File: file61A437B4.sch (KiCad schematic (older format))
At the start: 2 parts, among them J1 DB37_Male

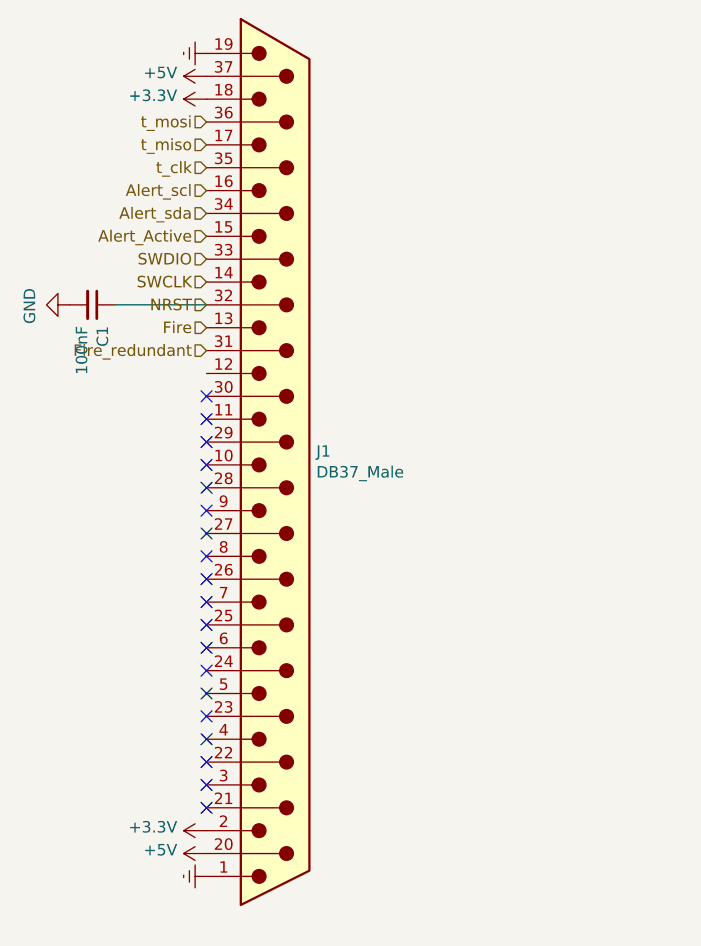
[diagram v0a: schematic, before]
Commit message: Updated PCB
Finalized most of the charges board and PCB
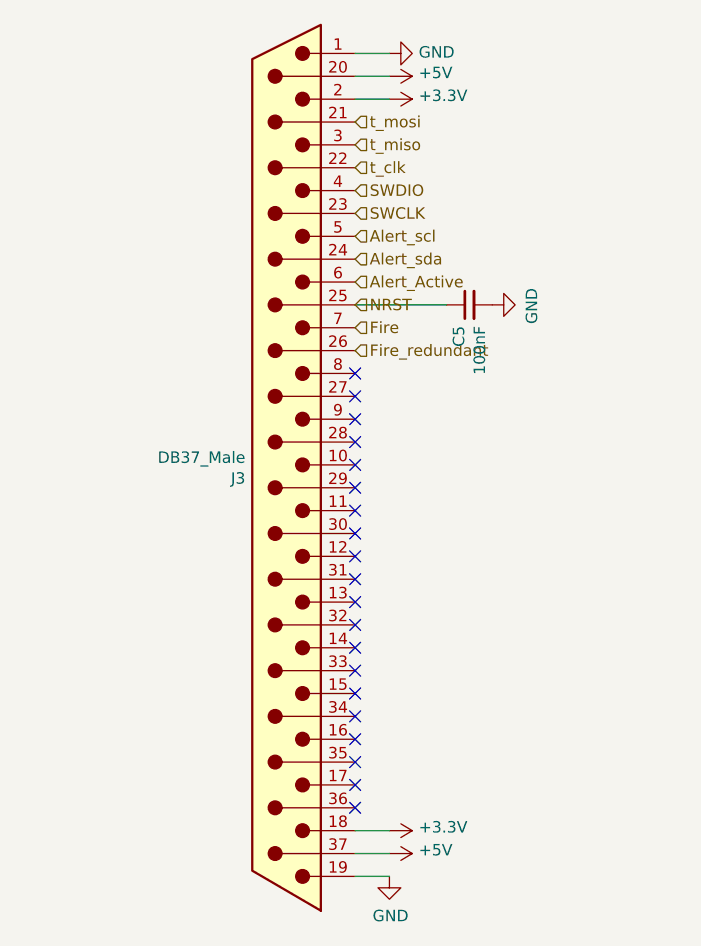
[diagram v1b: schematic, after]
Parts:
- C5: renamed from C1; footprint (none) -> Capacitor_SMD:C_0603_1608Metric
- J3: renamed from J1; footprint (none) -> Connector_Dsub:DSUB-37_Male_Horizontal_P2.77x2.54mm_EdgePinOffset9.40mm
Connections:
- net Earth is gone; now on net GND: J3.1, J3.19
- net Alert_Active: now also J3.6; no longer J3.15
- net Alert_scl: now also J3.5; no longer J3.16
- net Alert_sda: now also J3.24; no longer J3.34
- net Fire: now also J3.7; no longer J3.13
- net Fire_redundant: now also J3.26; no longer J3.31
- net NRST: now also J3.25; no longer J3.32
- net SWCLK: now also J3.23; no longer J3.14
- net SWDIO: now also J3.4; no longer J3.33
- net t_clk: now also J3.22; no longer J3.35
- net t_miso: now also J3.3; no longer J3.17
- net t_mosi: now also J3.21; no longer J3.36
- no-connect marks 19 -> 20
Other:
- moved on the sheet: C5, J3
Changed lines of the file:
@@
 $Descr A4 11693 8268
 encoding utf-8
-Sheet 4 4
+Sheet 2 4
 Title ""
 Date ""
@@
 $EndDescr
 $Comp
-L Connector:DB37_Male J1
+L Connector:DB37_Male J3
 U 1 1 61A44CBA
-P 5550 3300
-F 0 "J1" H 5730 3359 50  0000 L CNN
-F 1 "DB37_Male" H 5730 3268 50  0000 L CNN
-F 2 "" H 5550 3300 50  0001 C CNN
-F 3 " ~" H 5550 3300 50  0001 C CNN
-	1    5550 3300
-	1    0    0    -1
+P 5600 3300
+F 0 "J3" H 5780 3359 50  0000 L CNN
+F 1 "DB37_Male" H 5780 3268 50  0000 L CNN
+F 2 "Connector_Dsub:DSUB-37_Male_Horizontal_P2.77x2.54mm_EdgePinOffset9.40mm" H 5600 3300 50  0001 C CNN
+F 3 " ~" H 5600 3300 50  0001 C CNN
+	1    5600 3300
+	-1   0    0    1
 $EndComp
-$Comp
-L power:Earth #PWR0104
-U 1 1 61A472F3
-P 5250 1500
-F 0 "#PWR0104" H 5250 1250 50  0001 C CNN
-F 1 "Earth" H 5250 1350 50  0001 C CNN
-F 2 "" H 5250 1500 50  0001 C CNN
-F 3 "~" H 5250 1500 50  0001 C CNN
-	1    5250 1500
-	0    1    1    0
-$EndComp
-$Comp
-L power:Earth #PWR0105
-U 1 1 61A486AF
-P 5250 5100
-F 0 "#PWR0105" H 5250 4850 50  0001 C CNN
-F 1 "Earth" H 5250 4950 50  0001 C CNN
-F 2 "" H 5250 5100 50  0001 C CNN
-F 3 "~" H 5250 5100 50  0001 C CNN
-	1    5250 5100
-	0    1    1    0
-$EndComp
-$Comp
-L power:+5V #PWR0137
-U 1 1 61A491E6
-P 5250 1600
-F 0 "#PWR0137" H 5250 1450 50  0001 C CNN
-F 1 "+5V" V 5265 1728 50  0000 L CNN
-F 2 "" H 5250 1600 50  0001 C CNN
-F 3 "" H 5250 1600 50  0001 C CNN
-	1    5250 1600
-	0    -1   -1   0
-$EndComp
-$Comp
-L power:+5V #PWR0138
-U 1 1 61A49AB4
-P 5250 5000
-F 0 "#PWR0138" H 5250 4850 50  0001 C CNN
-F 1 "+5V" V 5265 5128 50  0000 L CNN
-F 2 "" H 5250 5000 50  0001 C CNN
-F 3 "" H 5250 5000 50  0001 C CNN
-	1    5250 5000
-	0    -1   -1   0
-$EndComp
-$Comp
-L power:+3.3V #PWR0139
-U 1 1 61A4A3FB
-P 5250 1700
-F 0 "#PWR0139" H 5250 1550 50  0001 C CNN
-F 1 "+3.3V" V 5265 1828 50  0000 L CNN
-F 2 "" H 5250 1700 50  0001 C CNN
-F 3 "" H 5250 1700 50  0001 C CNN
-	1    5250 1700
-	0    -1   -1   0
-$EndComp
-$Comp
-L power:+3.3V #PWR0140
-U 1 1 61A4AB5D
-P 5250 4900
-F 0 "#PWR0140" H 5250 4750 50  0001 C CNN
-F 1 "+3.3V" V 5265 5028 50  0000 L CNN
-F 2 "" H 5250 4900 50  0001 C CNN
-F 3 "" H 5250 4900 50  0001 C CNN
-	1    5250 4900
-	0    -1   -1   0
-$EndComp
-Text HLabel 5250 1800 0    50   Input ~ 0
+Text HLabel 5900 1800 2    50   Input ~ 0
 t_mosi
-Text HLabel 5250 1900 0    50   Input ~ 0
+Text HLabel 5900 1900 2    50   Input ~ 0
 t_miso
-Text HLabel 5250 2000 0    50   Input ~ 0
+Text HLabel 5900 2000 2    50   Input ~ 0
 t_clk
-Text HLabel 5250 2100 0    50   Input ~ 0
+Text HLabel 5900 2300 2    50   Input ~ 0
 Alert_scl
-Text HLabel 5250 2200 0    50   Input ~ 0
+Text HLabel 5900 2400 2    50   Input ~ 0
 Alert_sda
-Text HLabel 5250 2300 0    50   Input ~ 0
+Text HLabel 5900 2500 2    50   Input ~ 0
 Alert_Active
-Text HLabel 5250 2400 0    50   Input ~ 0
+Text HLabel 5900 2100 2    50   Input ~ 0
 SWDIO
-Text HLabel 5250 2500 0    50   Input ~ 0
+Text HLabel 5900 2200 2    50   Input ~ 0
 SWCLK
-Text HLabel 5250 2600 0    50   Input ~ 0
+Text HLabel 5900 2600 2    50   Input ~ 0
 NRST
-Text HLabel 5250 2700 0    50   Input ~ 0
+Text HLabel 5900 2700 2    50   Input ~ 0
 Fire
-Text HLabel 5250 2800 0    50   Input ~ 0
+Text HLabel 5900 2800 2    50   Input ~ 0
 Fire_redundant
-NoConn ~ 5250 3600
-NoConn ~ 5250 3500
-NoConn ~ 5250 3400
-NoConn ~ 5250 3300
-NoConn ~ 5250 3200
-NoConn ~ 5250 3100
-NoConn ~ 5250 3000
-NoConn ~ 5250 3800
-NoConn ~ 5250 3700
-NoConn ~ 5250 3900
-NoConn ~ 5250 4000
-NoConn ~ 5250 4100
-NoConn ~ 5250 4200
-NoConn ~ 5250 4300
-NoConn ~ 5250 4800
-NoConn ~ 5250 4700
-NoConn ~ 5250 4600
-NoConn ~ 5250 4500
-NoConn ~ 5250 4400
+NoConn ~ 5900 3600
+NoConn ~ 5900 3500
+NoConn ~ 5900 3400
+NoConn ~ 5900 3300
+NoConn ~ 5900 3200
+NoConn ~ 5900 3100
+NoConn ~ 5900 3000
+NoConn ~ 5900 3800
+NoConn ~ 5900 3700
+NoConn ~ 5900 3900
+NoConn ~ 5900 4000
+NoConn ~ 5900 4100
+NoConn ~ 5900 4200
+NoConn ~ 5900 4300
+NoConn ~ 5900 4800
+NoConn ~ 5900 4700
+NoConn ~ 5900 4600
+NoConn ~ 5900 4500
+NoConn ~ 5900 4400
 $Comp
 L power:GND #PWR?
 U 1 1 61A5558D
-P 4650 2600
+P 6500 2600
 AR Path="/61A5558D" Ref="#PWR?"  Part="1"
-AR Path="/61A437B5/61A5558D" Ref="#PWR0141"  Part="1"
-F 0 "#PWR0141" H 4650 2350 50  0001 C CNN
-F 1 "GND" H 4655 2427 50  0000 C CNN
-F 2 "" H 4650 2600 50  0001 C CNN
-F 3 "" H 4650 2600 50  0001 C CNN
-	1    4650 2600
-	0    1    1    0
+AR Path="/61A437B5/61A5558D" Ref="#PWR025"  Part="1"
+F 0 "#PWR025" H 6500 2350 50  0001 C CNN
+F 1 "GND" H 6505 2427 50  0000 C CNN
+F 2 "" H 6500 2600 50  0001 C CNN
+F 3 "" H 6500 2600 50  0001 C CNN
+	1    6500 2600
+	0    -1   1    0
 $EndComp
 $Comp
 L Device:C_Small C?
 U 1 1 61A55586
-P 4750 2600
+P 6400 2600
 AR Path="/61A55586" Ref="C?"  Part="1"
-AR Path="/61A437B5/61A55586" Ref="C1"  Part="1"
-F 0 "C1" H 4842 2646 50  0000 L CNN
-F 1 "100nF" H 4842 2555 50  0000 L CNN
-F 2 "" H 4750 2600 50  0001 C CNN
-F 3 "~" H 4750 2600 50  0001 C CNN
-	1    4750 2600
-	0    1    1    0
+AR Path="/61A437B5/61A55586" Ref="C5"  Part="1"
+F 0 "C5" H 6492 2646 50  0000 L CNN
+F 1 "100nF" H 6492 2555 50  0000 L CNN
+F 2 "Capacitor_SMD:C_0603_1608Metric" H 6400 2600 50  0001 C CNN
+F 3 "~" H 6400 2600 50  0001 C CNN
+	1    6400 2600
+	0    -1   1    0
 $EndComp
 Wire Wire Line
-	4850 2600 5250 2600
+	6300 2600 5900 2600
+Wire Wire Line
+	6050 4900 5900 4900
+Wire Wire Line
+	6050 5000 5900 5000
+Wire Wire Line
+	6050 1500 5900 1500
+Wire Wire Line
+	6050 1600 5900 1600
+Wire Wire Line
+	6050 1700 5900 1700
+Wire Wire Line
+	6050 5100 5900 5100
+$Comp
+L power:+3.3V #PWR028
+U 1 1 61A4A3FB
+P 6050 1700
+F 0 "#PWR028" H 6050 1550 50  0001 C CNN
+F 1 "+3.3V" V 6065 1828 50  0000 L CNN
+F 2 "" H 6050 1700 50  0001 C CNN
+F 3 "" H 6050 1700 50  0001 C CNN
+	1    6050 1700
+	0    1    -1   0
+$EndComp
+$Comp
+L power:+5V #PWR027
+U 1 1 61A491E6
+P 6050 1600
+F 0 "#PWR027" H 6050 1450 50  0001 C CNN
+F 1 "+5V" V 6065 1728 50  0000 L CNN
+F 2 "" H 6050 1600 50  0001 C CNN
+F 3 "" H 6050 1600 50  0001 C CNN
+	1    6050 1600
+	0    1    -1   0
+$EndComp
+$Comp
+L power:+5V #PWR0104
+U 1 1 61A49AB4
+P 6050 5000
+F 0 "#PWR0104" H 6050 4850 50  0001 C CNN
+F 1 "+5V" V 6065 5128 50  0000 L CNN
+F 2 "" H 6050 5000 50  0001 C CNN
+F 3 "" H 6050 5000 50  0001 C CNN
+	1    6050 5000
+	0    1    -1   0
+$EndComp
+$Comp
+L power:+3.3V #PWR0105
+U 1 1 61A4AB5D
+P 6050 4900
+F 0 "#PWR0105" H 6050 4750 50  0001 C CNN
+F 1 "+3.3V" V 6065 5028 50  0000 L CNN
+F 2 "" H 6050 4900 50  0001 C CNN
+F 3 "" H 6050 4900 50  0001 C CNN
+	1    6050 4900
+	0    1    -1   0
+$EndComp
+NoConn ~ 5900 2900
+$Comp
+L power:GND #PWR0114
+U 1 1 61CFE017
+P 6050 5100
+F 0 "#PWR0114" H 6050 4850 50  0001 C CNN
+F 1 "GND" H 6055 4927 50  0000 C CNN
+F 2 "" H 6050 5100 50  0001 C CNN
+F 3 "" H 6050 5100 50  0001 C CNN
+	1    6050 5100
+	1    0    0    -1
+$EndComp
+$Comp
+L power:GND #PWR0115
+U 1 1 61CFEBAB
+P 6050 1500
+F 0 "#PWR0115" H 6050 1250 50  0001 C CNN
+F 1 "GND" V 6055 1372 50  0000 R CNN
+F 2 "" H 6050 1500 50  0001 C CNN
+F 3 "" H 6050 1500 50  0001 C CNN
+	1    6050 1500
+	0    -1   -1   0
+$EndComp
 $EndSCHEMATC

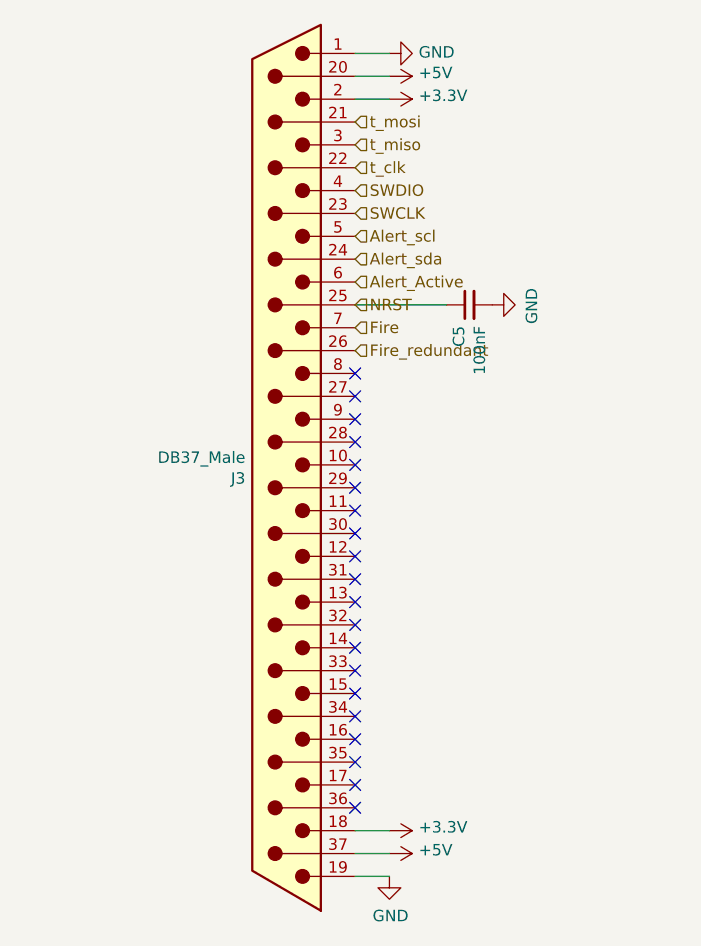
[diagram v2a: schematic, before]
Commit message: updated pcb
pcb updated to the right size
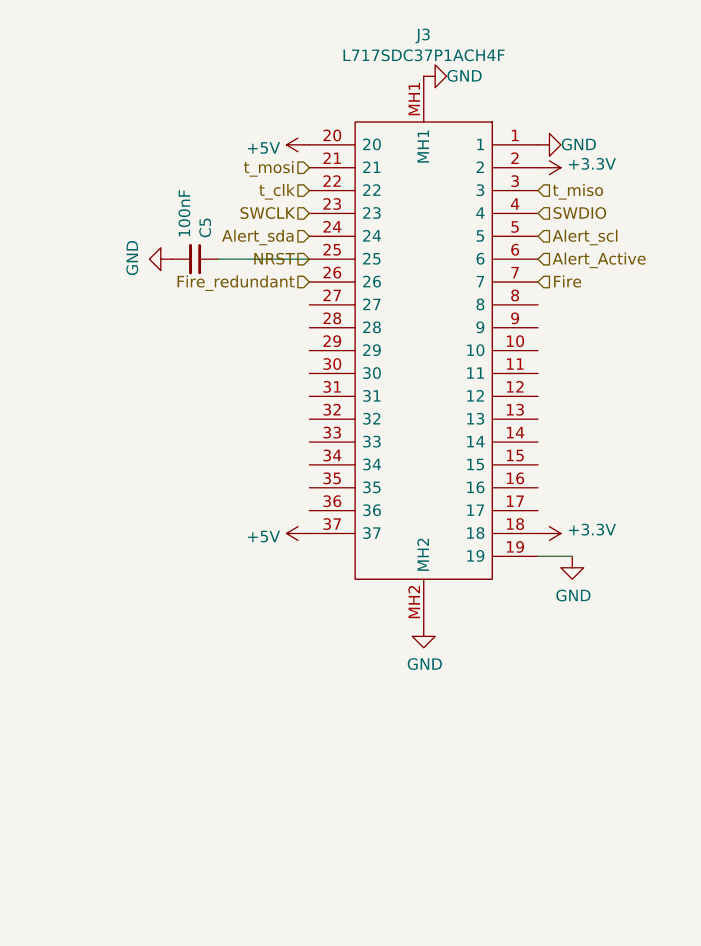
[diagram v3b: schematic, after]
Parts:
- removed J3: DB37_Male, Connector_Dsub:DSUB-37_Male_Horizontal_P2.77x2.54mm_EdgePinOffset9.40mm, symbol Connector:DB37_Male
- added J3: L717SDC37P1ACH4F, SamacSys_Parts:L717SDC37P1ACH4F, symbol SamacSys_Parts:L717SDC37P1ACH4F
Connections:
- net +3V3: now also J3.18, J3.2
- net +5V: now also J3.20, J3.37
- net Alert_Active: now also J3.6
- net Alert_scl: now also J3.5
- net Alert_sda: now also J3.24
- net Fire: now also J3.7
- net Fire_redundant: now also J3.26
- net GND: now also J3.1, J3.19, J3.MH1, J3.MH2
- net NRST: now also J3.25
- net SWCLK: now also J3.23
- net SWDIO: now also J3.4
- net t_clk: now also J3.22
- net t_miso: now also J3.3
- net t_mosi: now also J3.21
- no-connect marks 20 -> 0
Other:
- moved on the sheet: C5
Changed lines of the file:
@@
 Comment4 ""
 $EndDescr
-$Comp
-L Connector:DB37_Male J3
-U 1 1 61A44CBA
-P 5600 3300
-F 0 "J3" H 5780 3359 50  0000 L CNN
-F 1 "DB37_Male" H 5780 3268 50  0000 L CNN
-F 2 "Connector_Dsub:DSUB-37_Male_Horizontal_P2.77x2.54mm_EdgePinOffset9.40mm" H 5600 3300 50  0001 C CNN
-F 3 " ~" H 5600 3300 50  0001 C CNN
-	1    5600 3300
-	-1   0    0    1
-$EndComp
-Text HLabel 5900 1800 2    50   Input ~ 0
+Text HLabel 5700 2000 0    50   Input ~ 0
 t_mosi
-Text HLabel 5900 1900 2    50   Input ~ 0
+Text HLabel 6700 2100 2    50   Input ~ 0
 t_miso
-Text HLabel 5900 2000 2    50   Input ~ 0
+Text HLabel 5700 2100 0    50   Input ~ 0
 t_clk
-Text HLabel 5900 2300 2    50   Input ~ 0
+Text HLabel 6700 2300 2    50   Input ~ 0
 Alert_scl
-Text HLabel 5900 2400 2    50   Input ~ 0
+Text HLabel 5700 2300 0    50   Input ~ 0
 Alert_sda
-Text HLabel 5900 2500 2    50   Input ~ 0
+Text HLabel 6700 2400 2    50   Input ~ 0
 Alert_Active
-Text HLabel 5900 2100 2    50   Input ~ 0
+Text HLabel 6700 2200 2    50   Input ~ 0
 SWDIO
-Text HLabel 5900 2200 2    50   Input ~ 0
+Text HLabel 5700 2200 0    50   Input ~ 0
 SWCLK
-Text HLabel 5900 2600 2    50   Input ~ 0
+Text HLabel 5700 2400 0    50   Input ~ 0
 NRST
-Text HLabel 5900 2700 2    50   Input ~ 0
+Text HLabel 6700 2500 2    50   Input ~ 0
 Fire
-Text HLabel 5900 2800 2    50   Input ~ 0
+Text HLabel 5700 2500 0    50   Input ~ 0
 Fire_redundant
-NoConn ~ 5900 3600
-NoConn ~ 5900 3500
-NoConn ~ 5900 3400
-NoConn ~ 5900 3300
-NoConn ~ 5900 3200
-NoConn ~ 5900 3100
-NoConn ~ 5900 3000
-NoConn ~ 5900 3800
-NoConn ~ 5900 3700
-NoConn ~ 5900 3900
-NoConn ~ 5900 4000
-NoConn ~ 5900 4100
-NoConn ~ 5900 4200
-NoConn ~ 5900 4300
-NoConn ~ 5900 4800
-NoConn ~ 5900 4700
-NoConn ~ 5900 4600
-NoConn ~ 5900 4500
-NoConn ~ 5900 4400
 $Comp
 L power:GND #PWR?
 U 1 1 61A5558D
-P 6500 2600
+P 5100 2400
 AR Path="/61A5558D" Ref="#PWR?"  Part="1"
-AR Path="/61A437B5/61A5558D" Ref="#PWR029"  Part="1"
-F 0 "#PWR029" H 6500 2350 50  0001 C CNN
-F 1 "GND" H 6505 2427 50  0000 C CNN
-F 2 "" H 6500 2600 50  0001 C CNN
-F 3 "" H 6500 2600 50  0001 C CNN
-	1    6500 2600
-	0    -1   1    0
+AR Path="/61A437B5/61A5558D" Ref="#PWR023"  Part="1"
+F 0 "#PWR023" H 5100 2150 50  0001 C CNN
+F 1 "GND" H 5105 2227 50  0000 C CNN
+F 2 "" H 5100 2400 50  0001 C CNN
+F 3 "" H 5100 2400 50  0001 C CNN
+	1    5100 2400
+	0    1    -1   0
 $EndComp
 $Comp
 L Device:C_Small C?
 U 1 1 61A55586
-P 6400 2600
+P 5200 2400
 AR Path="/61A55586" Ref="C?"  Part="1"
 AR Path="/61A437B5/61A55586" Ref="C5"  Part="1"
-F 0 "C5" H 6492 2646 50  0000 L CNN
-F 1 "100nF" H 6492 2555 50  0000 L CNN
-F 2 "Capacitor_SMD:C_0603_1608Metric" H 6400 2600 50  0001 C CNN
-F 3 "~" H 6400 2600 50  0001 C CNN
-	1    6400 2600
-	0    -1   1    0
+F 0 "C5" H 5292 2446 50  0000 L CNN
+F 1 "100nF" H 5292 2355 50  0000 L CNN
+F 2 "Capacitor_SMD:C_0603_1608Metric" H 5200 2400 50  0001 C CNN
+F 3 "~" H 5200 2400 50  0001 C CNN
+	1    5200 2400
+	0    1    -1   0
 $EndComp
 Wire Wire Line
-	6300 2600 5900 2600
-Wire Wire Line
-	6050 4900 5900 4900
-Wire Wire Line
-	6050 5000 5900 5000
-Wire Wire Line
-	6050 1500 5900 1500
-Wire Wire Line
-	6050 1600 5900 1600
-Wire Wire Line
-	6050 1700 5900 1700
-Wire Wire Line
-	6050 5100 5900 5100
+	5300 2400 5700 2400
 $Comp
-L power:+3.3V #PWR025
+L power:+3.3V #PWR029
 U 1 1 61A4A3FB
-P 6050 1700
-F 0 "#PWR025" H 6050 1550 50  0001 C CNN
-F 1 "+3.3V" V 6065 1828 50  0000 L CNN
-F 2 "" H 6050 1700 50  0001 C CNN
-F 3 "" H 6050 1700 50  0001 C CNN
-	1    6050 1700
+P 6700 2000
+F 0 "#PWR029" H 6700 1850 50  0001 C CNN
+F 1 "+3.3V" V 6715 2128 50  0000 L CNN
+F 2 "" H 6700 2000 50  0001 C CNN
+F 3 "" H 6700 2000 50  0001 C CNN
+	1    6700 2000
 	0    1    -1   0
 $EndComp
@@
 L power:+5V #PWR024
 U 1 1 61A491E6
-P 6050 1600
-F 0 "#PWR024" H 6050 1450 50  0001 C CNN
-F 1 "+5V" V 6065 1728 50  0000 L CNN
-F 2 "" H 6050 1600 50  0001 C CNN
-F 3 "" H 6050 1600 50  0001 C CNN
-	1    6050 1600
+P 5700 1900
+F 0 "#PWR024" H 5700 1750 50  0001 C CNN
+F 1 "+5V" V 5715 2028 50  0000 L CNN
+F 2 "" H 5700 1900 50  0001 C CNN
+F 3 "" H 5700 1900 50  0001 C CNN
+	1    5700 1900
+	0    -1   1    0
+$EndComp
+$Comp
+L power:+3.3V #PWR030
+U 1 1 61A4AB5D
+P 6700 3600
+F 0 "#PWR030" H 6700 3450 50  0001 C CNN
+F 1 "+3.3V" V 6715 3728 50  0000 L CNN
+F 2 "" H 6700 3600 50  0001 C CNN
+F 3 "" H 6700 3600 50  0001 C CNN
+	1    6700 3600
 	0    1    -1   0
 $EndComp
 $Comp
-L power:+5V #PWR027
-U 1 1 61A49AB4
-P 6050 5000
-F 0 "#PWR027" H 6050 4850 50  0001 C CNN
-F 1 "+5V" V 6065 5128 50  0000 L CNN
-F 2 "" H 6050 5000 50  0001 C CNN
-F 3 "" H 6050 5000 50  0001 C CNN
-	1    6050 5000
-	0    1    -1   0
+L power:GND #PWR026
+U 1 1 61CFEBAB
+P 6200 1600
+F 0 "#PWR026" H 6200 1350 50  0001 C CNN
+F 1 "GND" V 6200 1500 50  0000 R CNN
+F 2 "" H 6200 1600 50  0001 C CNN
+F 3 "" H 6200 1600 50  0001 C CNN
+	1    6200 1600
+	0    -1   -1   0
 $EndComp
 $Comp
-L power:+3.3V #PWR026
-U 1 1 61A4AB5D
-P 6050 4900
-F 0 "#PWR026" H 6050 4750 50  0001 C CNN
-F 1 "+3.3V" V 6065 5028 50  0000 L CNN
-F 2 "" H 6050 4900 50  0001 C CNN
-F 3 "" H 6050 4900 50  0001 C CNN
-	1    6050 4900
-	0    1    -1   0
+L SamacSys_Parts:L717SDC37P1ACH4F J3
+U 1 1 61D5E9EE
+P 6200 1600
+F 0 "J3" V 6019 1600 50  0000 C CNN
+F 1 "L717SDC37P1ACH4F" V 6110 1600 50  0000 C CNN
+F 2 "SamacSys_Parts:L717SDC37P1ACH4F" H 8450 1900 50  0001 L CNN
+F 3 "https://cdn.amphenol-icc.com/media/wysiwyg/files/drawing/l717sdxxxp1ach4f.pdf" H 8450 1800 50  0001 L CNN
+F 4 "D-Sub Standard Connectors 37P Sz C Std Density Pin Screwlock 4-40" H 8450 1700 50  0001 L CNN "Description"
+F 5 "12.93" H 8450 1600 50  0001 L CNN "Height"
+F 6 "523-L717SDC37P1ACH4F" H 8450 1500 50  0001 L CNN "Mouser Part Number"
+F 7 "https://www.mouser.co.uk/ProductDetail/Amphenol-Commercial-Products/L717SDC37P1ACH4F?qs=wLKqLMNa9uLzTtnbxoO2Ng%3D%3D" H 8450 1400 50  0001 L CNN "Mouser Price/Stock"
+F 8 "Amphenol" H 8450 1300 50  0001 L CNN "Manufacturer_Name"
+F 9 "L717SDC37P1ACH4F" H 8450 1200 50  0001 L CNN "Manufacturer_Part_Number"
+	1    6200 1600
+	0    1    1    0
 $EndComp
-NoConn ~ 5900 2900
 $Comp
 L power:GND #PWR028
+U 1 1 61D612F7
+P 6700 1900
+F 0 "#PWR028" H 6700 1650 50  0001 C CNN
+F 1 "GND" V 6700 1800 50  0000 R CNN
+F 2 "" H 6700 1900 50  0001 C CNN
+F 3 "" H 6700 1900 50  0001 C CNN
+	1    6700 1900
+	0    -1   -1   0
+$EndComp
+$Comp
+L power:GND #PWR031
 U 1 1 61CFE017
-P 6050 5100
-F 0 "#PWR028" H 6050 4850 50  0001 C CNN
-F 1 "GND" H 6055 4927 50  0000 C CNN
-F 2 "" H 6050 5100 50  0001 C CNN
-F 3 "" H 6050 5100 50  0001 C CNN
-	1    6050 5100
+P 6850 3700
+F 0 "#PWR031" H 6850 3450 50  0001 C CNN
+F 1 "GND" H 6855 3527 50  0000 C CNN
+F 2 "" H 6850 3700 50  0001 C CNN
+F 3 "" H 6850 3700 50  0001 C CNN
+	1    6850 3700
+	1    0    0    -1
+$EndComp
+Wire Wire Line
+	6850 3700 6700 3700
+$Comp
+L power:GND #PWR027
+U 1 1 61D6677B
+P 6200 4000
+F 0 "#PWR027" H 6200 3750 50  0001 C CNN
+F 1 "GND" H 6205 3827 50  0000 C CNN
+F 2 "" H 6200 4000 50  0001 C CNN
+F 3 "" H 6200 4000 50  0001 C CNN
+	1    6200 4000
 	1    0    0    -1
 $EndComp
 $Comp
-L power:GND #PWR023
-U 1 1 61CFEBAB
-P 6050 1500
-F 0 "#PWR023" H 6050 1250 50  0001 C CNN
-F 1 "GND" V 6055 1372 50  0000 R CNN
-F 2 "" H 6050 1500 50  0001 C CNN
-F 3 "" H 6050 1500 50  0001 C CNN
-	1    6050 1500
-	0    -1   -1   0
+L power:+5V #PWR025
+U 1 1 61A49AB4
+P 5700 3600
+F 0 "#PWR025" H 5700 3450 50  0001 C CNN
+F 1 "+5V" V 5715 3728 50  0000 L CNN
+F 2 "" H 5700 3600 50  0001 C CNN
+F 3 "" H 5700 3600 50  0001 C CNN
+	1    5700 3600
+	0    -1   1    0
 $EndComp
 $EndSCHEMATC
